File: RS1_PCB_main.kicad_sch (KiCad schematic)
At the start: 50 parts, among them J1 Conn_01x05, J3 Connector, USB-TYPE-C-16P, J4 Conn_01x10_Pin, J5 Conn_01x02, J7 Conn_01x02, J8 Conn_01x02, Q4 2N7002, SW3 GT-TC172A-H035-L1 (PWR BTN), U1 ESP32-C6-WROOM-1, U17 ME6217C33M5G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

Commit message: all connected
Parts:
- removed J4: Conn_01x10_Pin, Connector_PinHeader_2.54mm:PinHeader_1x10_P2.54mm_Vertical, symbol Connector:Conn_01x10_Pin

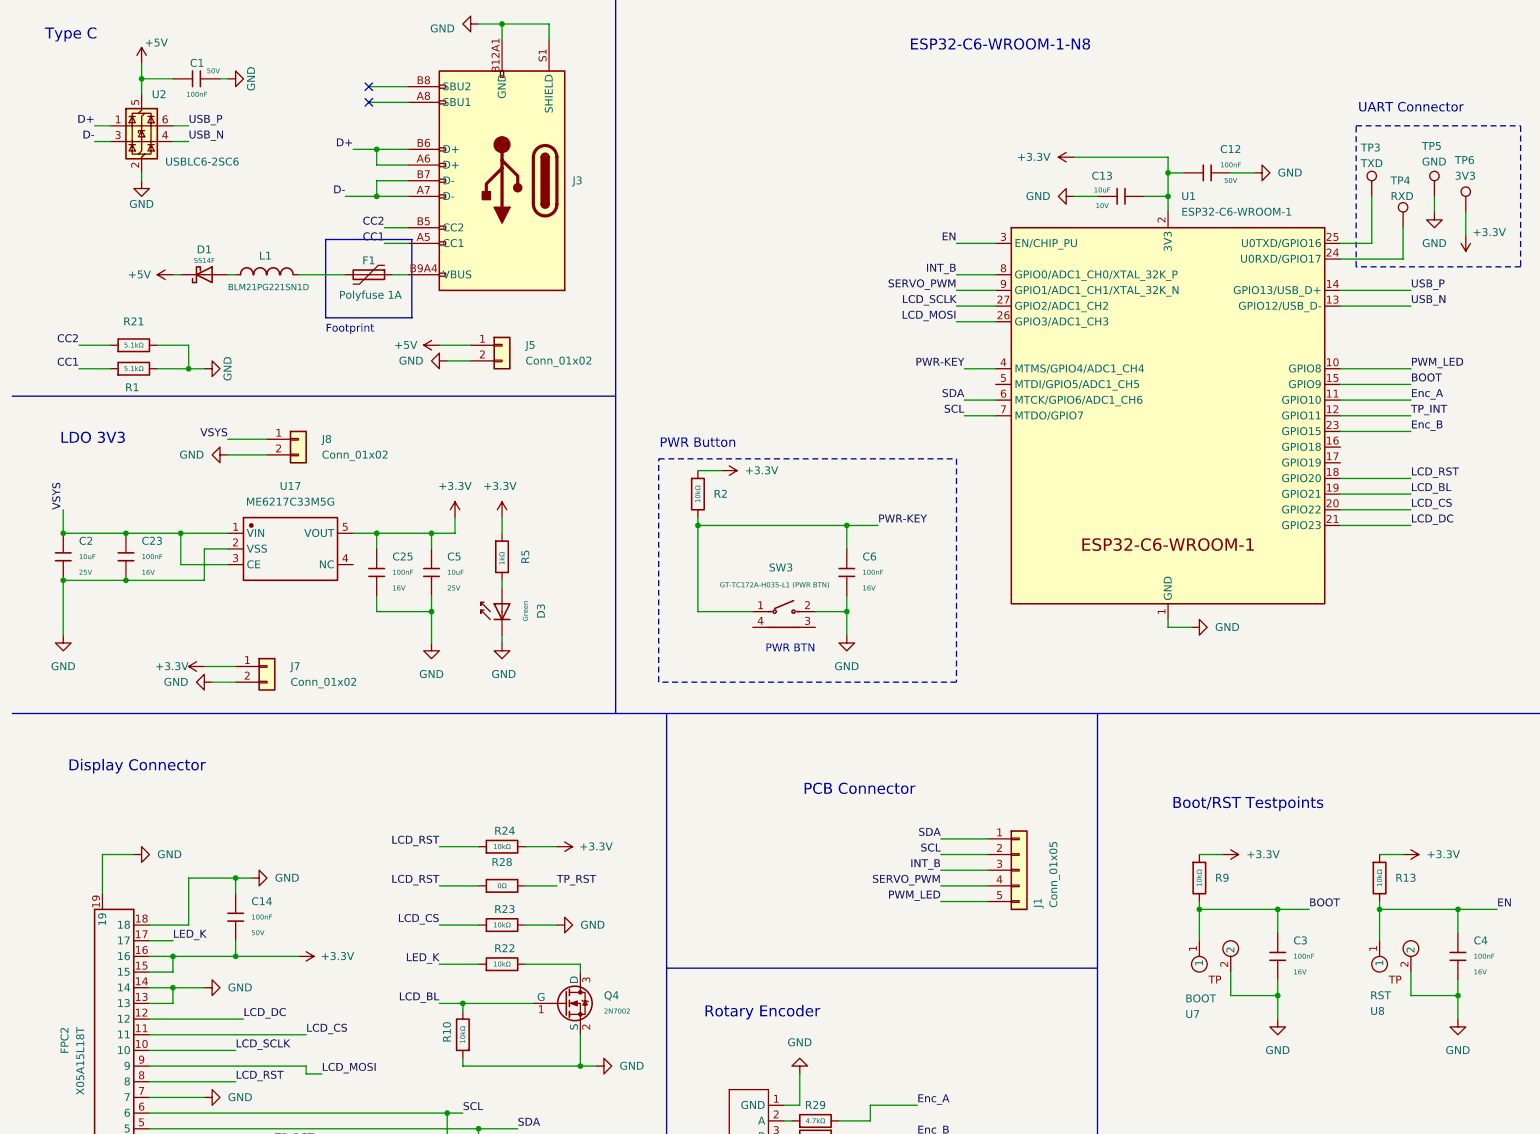
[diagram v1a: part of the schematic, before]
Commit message: changed testpoints, worked on silkprints
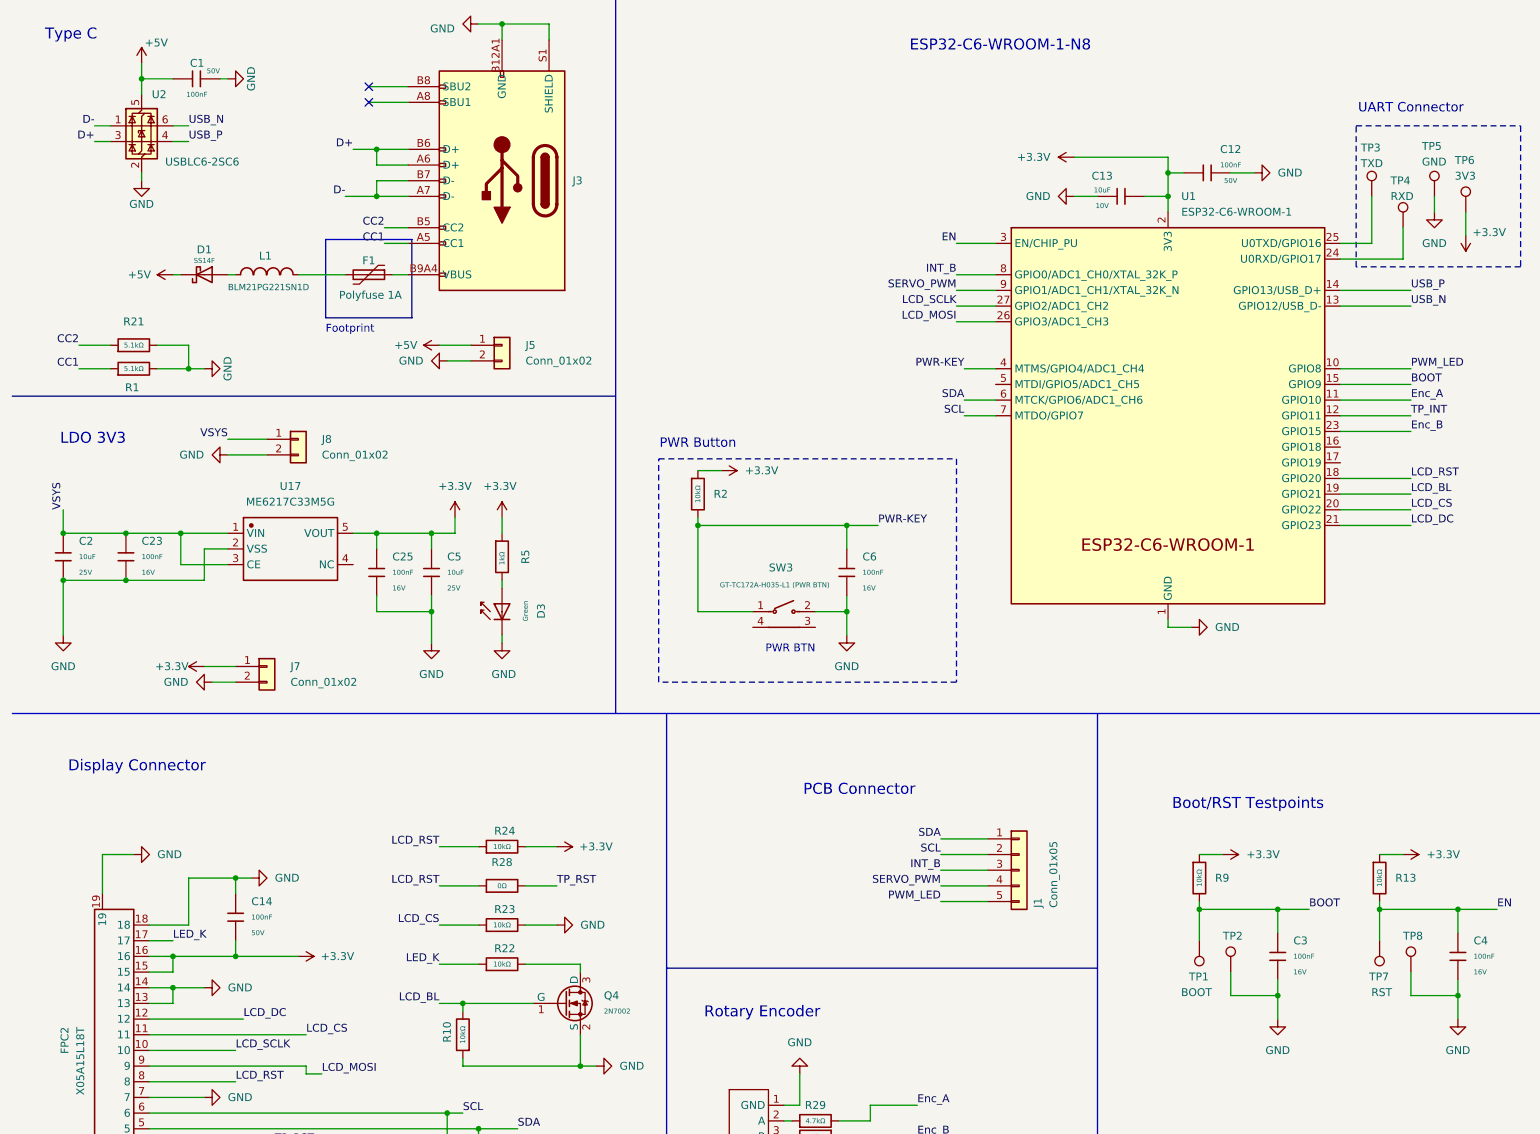
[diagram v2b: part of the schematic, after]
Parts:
- removed U7: BOOT, ESP32_C6_libfoot:TP_1.75mm_2Points, symbol ESP32_C6_Lib:TP_1.75mm_2Points
- removed U8: RST, ESP32_C6_libfoot:TP_1.75mm_2Points, symbol ESP32_C6_Lib:TP_1.75mm_2Points
- added TP1: BOOT, TestPoint:TestPoint_Pad_D1.5mm, symbol Connector:TestPoint
- added TP2, TP8: -, TestPoint:TestPoint_Pad_D1.5mm, symbol Connector:TestPoint
- added TP7: RST, TestPoint:TestPoint_Pad_D1.5mm, symbol Connector:TestPoint
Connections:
- net BOOT: now also TP1.1
- net D+: now also U2.3 (I/O2); no longer U2.1 (I/O1)
- net D-: now also U2.1 (I/O1); no longer U2.3 (I/O2)
- net EN: now also TP7.1
- net GND: now also TP2.1, TP8.1
- net USB_N: now also U2.6 (I/O1); no longer U2.4 (I/O2)
- net USB_P: now also U2.4 (I/O2); no longer U2.6 (I/O1)
